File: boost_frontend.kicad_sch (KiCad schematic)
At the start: 28 parts, among them Q1 NVTFS5C453NLWFTAG, U6 LT8342RV-TRMPBF

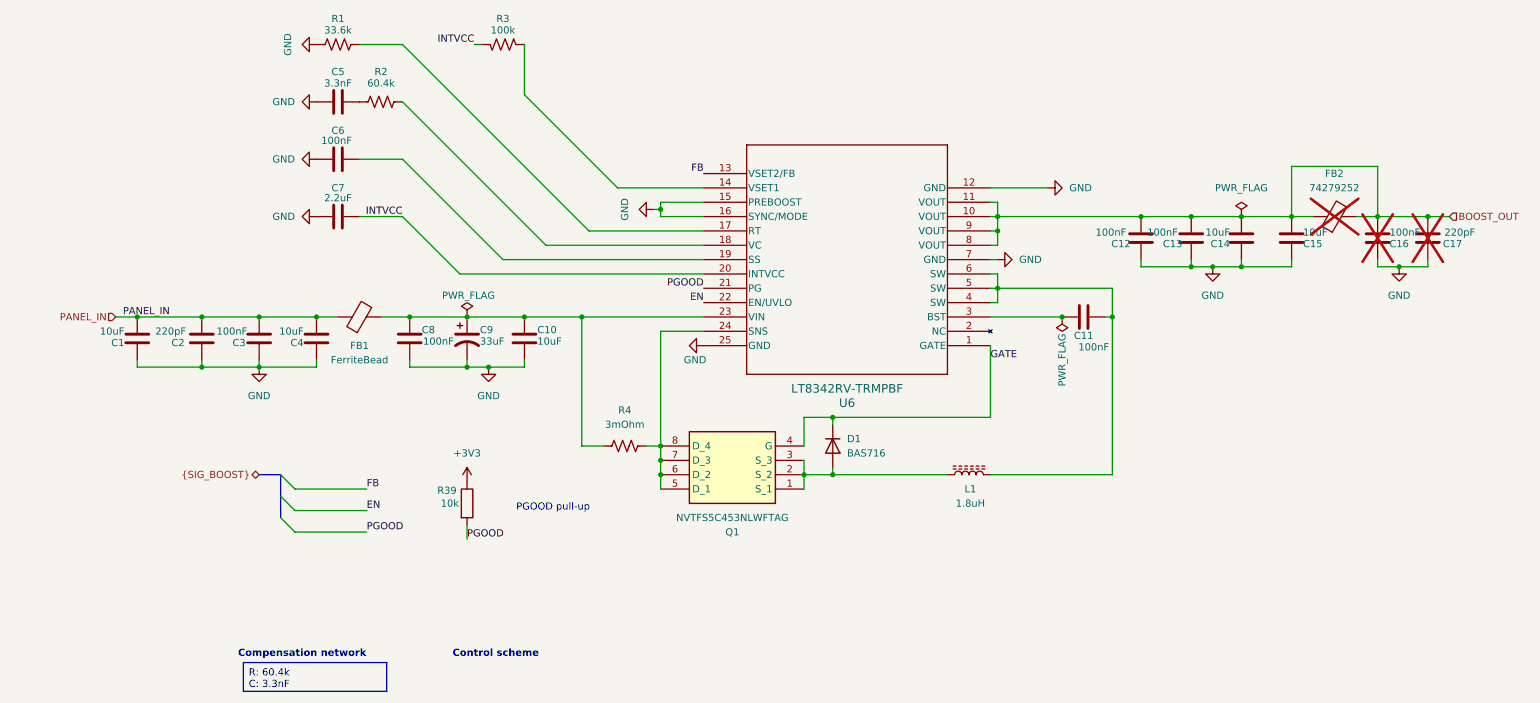
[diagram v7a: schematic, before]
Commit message: Schematic updates
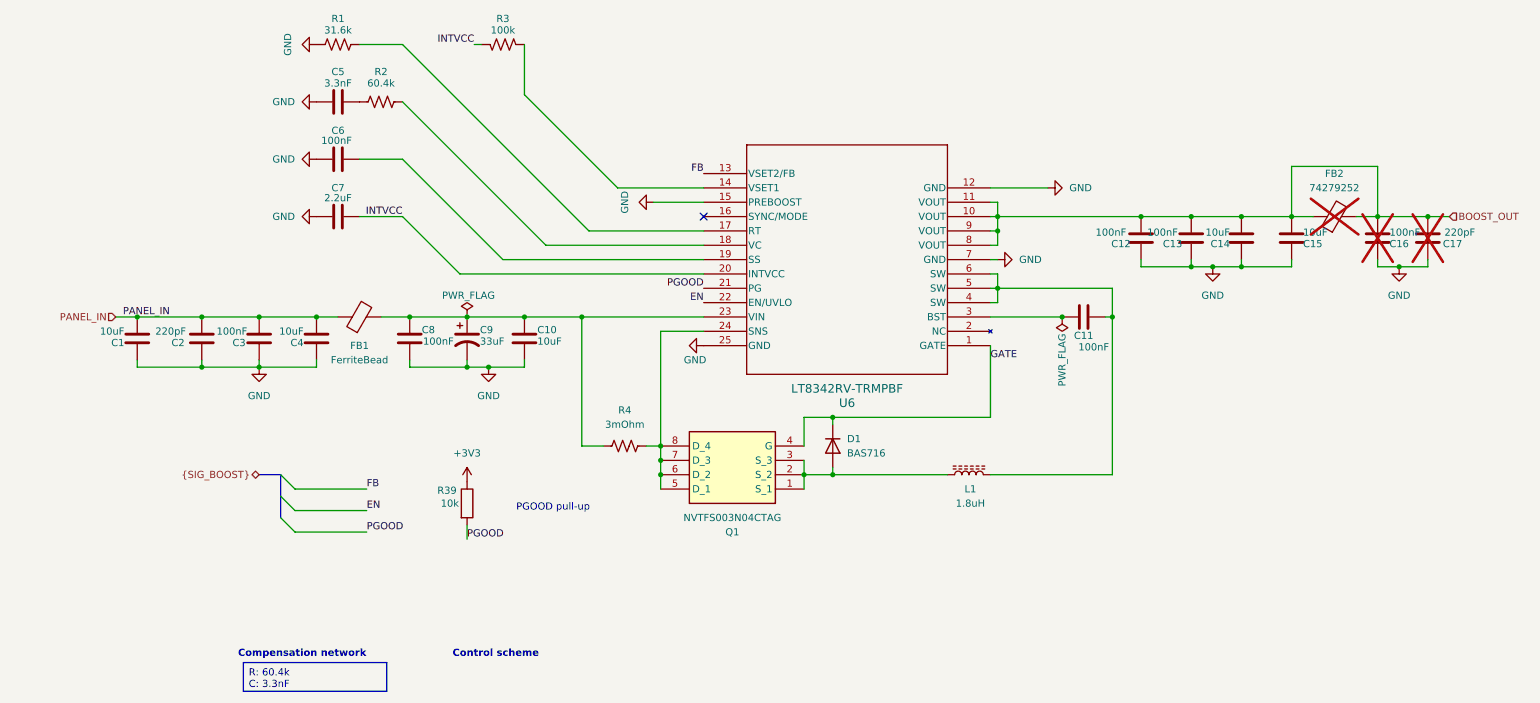
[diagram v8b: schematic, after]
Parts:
- C2: Mfr Murata Electronics -> Samsung Electro-Mechanics
- C5: Mfr Murata Electronics -> TDK; Mfr P/N CL10B333KB8NNNC -> C1608C0G1H332JT000N; Supplier_1 P/N C21117 -> C342849; Supplier_1 Price @ Qty 1 -> (none)
- C6: Mfr KYOCERA AVX -> YAGEO; Supplier_1 Price @ Qty 1 -> (none)
- C7, R3: Supplier_1 Price @ Qty 1 -> (none)
- D1: Mfr (none) -> Nexperia; Supplier_1 P/N C5292819 -> C282366
- L1: Mfr P/N SER2918H-333KL -> XEL6060-272MEC; Supplier_1 P/N C3911813 -> C19191641; Supplier_1 Price @ Qty 1 -> (none); Supplier_2 JLCPCB -> (none); Supplier_2 P/N C19191693 -> (none); Supplier_2 Price @ Qty 1 -> (none); Supplier_2 Unit Price 1.5264 -> (none)
- Q1: value NVTFS5C453NLWFTAG -> NVTFS003N04CTAG; Manufacturer_Name onsemi -> (none); Manufacturer_Part_Number NVTFS5C453NLWFTAG -> (none); Mfr (none) -> onsemi; Mfr P/N (none) -> NVTFS003N04CTAG; Mouser Part Number 863-NVTFS5C453NLWFTA -> (none); Mouser Price/Stock https://www.mouser.co.uk/ProductDetail/ON-Semiconductor/NVT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 -> (none); Supplier_1 P/N C145551 -> C604632
- R1: value 33.6k -> 31.6k; Mfr KOA Speer Electronics, Inc. -> YAGEO; Mfr P/N RN73R1JTTD3362B25 -> RT0603BRD0731K6L; Supplier_1 P/N C22800 -> C705766; Supplier_1 Price @ Qty 1 -> (none)
- R2: Mfr KOA Speer Electronics, Inc. -> UNI-ROYAL(Uniroyal Elec); Mfr P/N RN73H1JTTD6042B25 -> 0603WAF6042T5E; Supplier_1 P/N C23228 -> C23089; Supplier_1 Price @ Qty 1 -> (none)
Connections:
- net GND: no longer U6.16 (SYNC/MODE)
- no-connect marks 0 -> 1
